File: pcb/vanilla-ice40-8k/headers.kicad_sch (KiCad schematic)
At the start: 4 parts, among them J1 QSH-060-01-L-D-A, J2 QSH-060-01-L-D-A, J3 QTH-060-01-L-D-A, J4 QTH-060-01-L-D-A

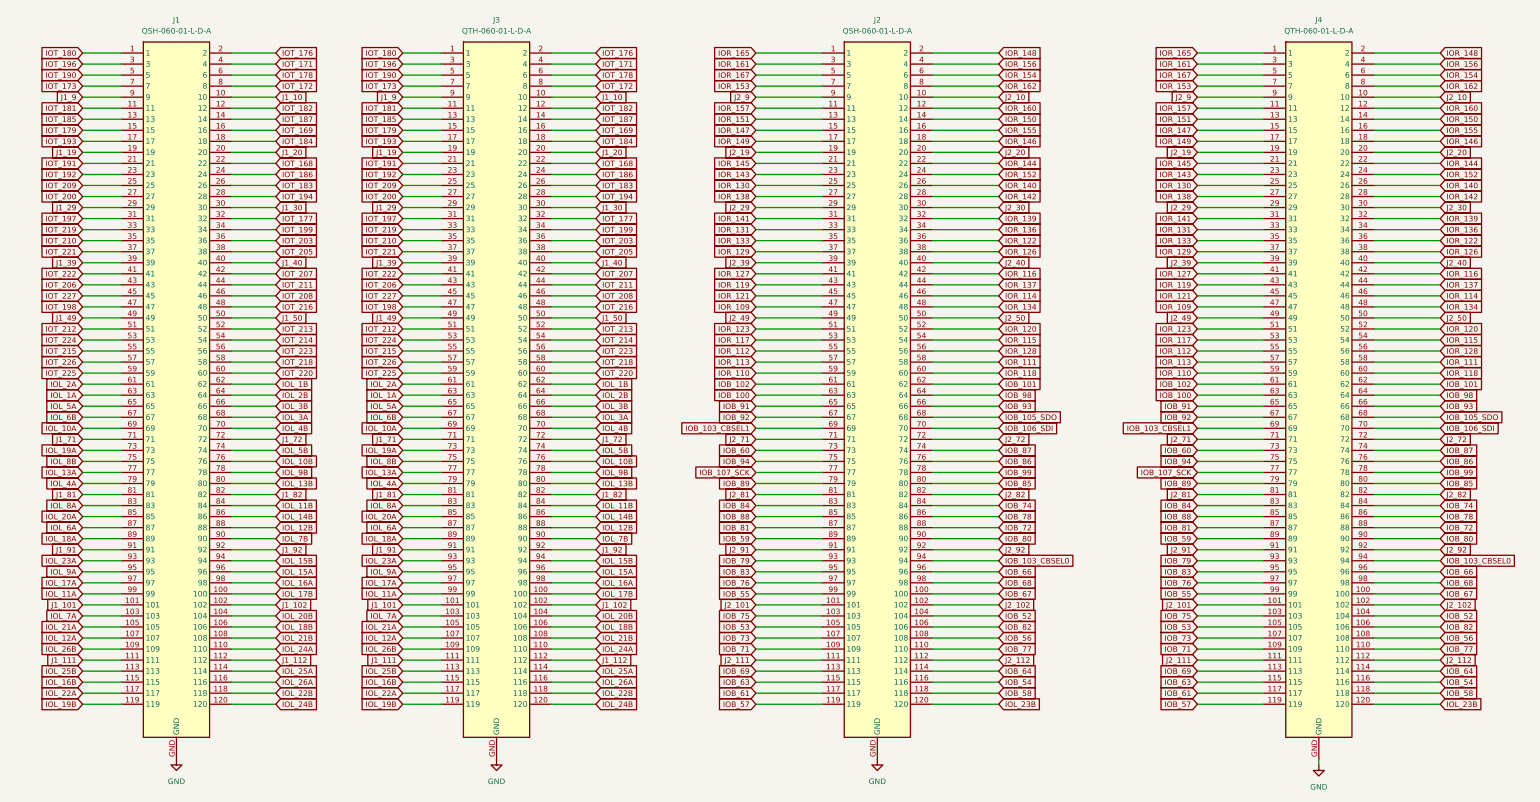
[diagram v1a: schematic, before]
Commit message: [hx8k][pcb] convert all components to custom lib
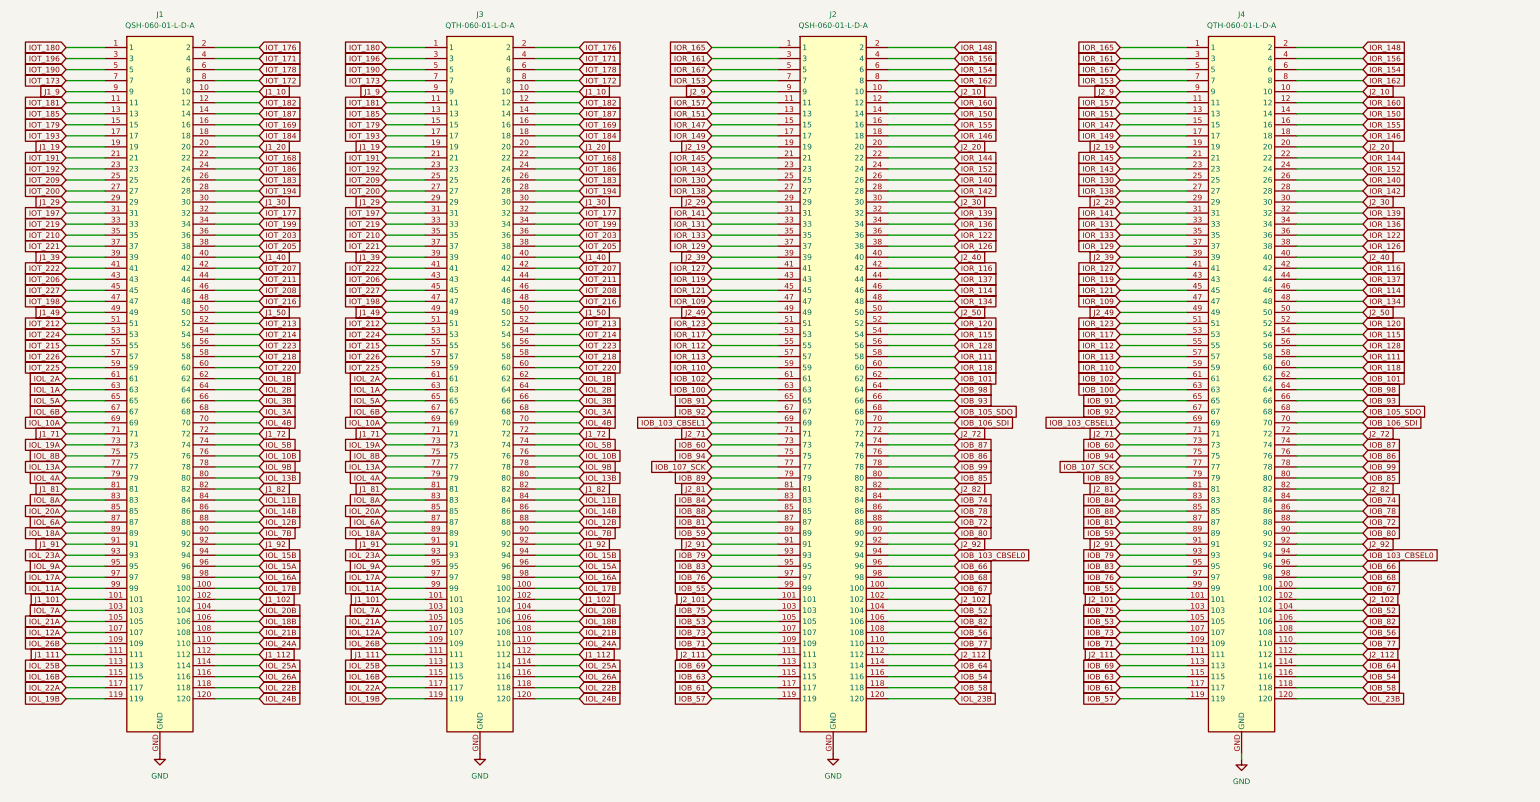
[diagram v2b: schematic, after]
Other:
- moved on the sheet: J1, J2, J3, J4

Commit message: [pcb][hx8k] add 3v3 to headers
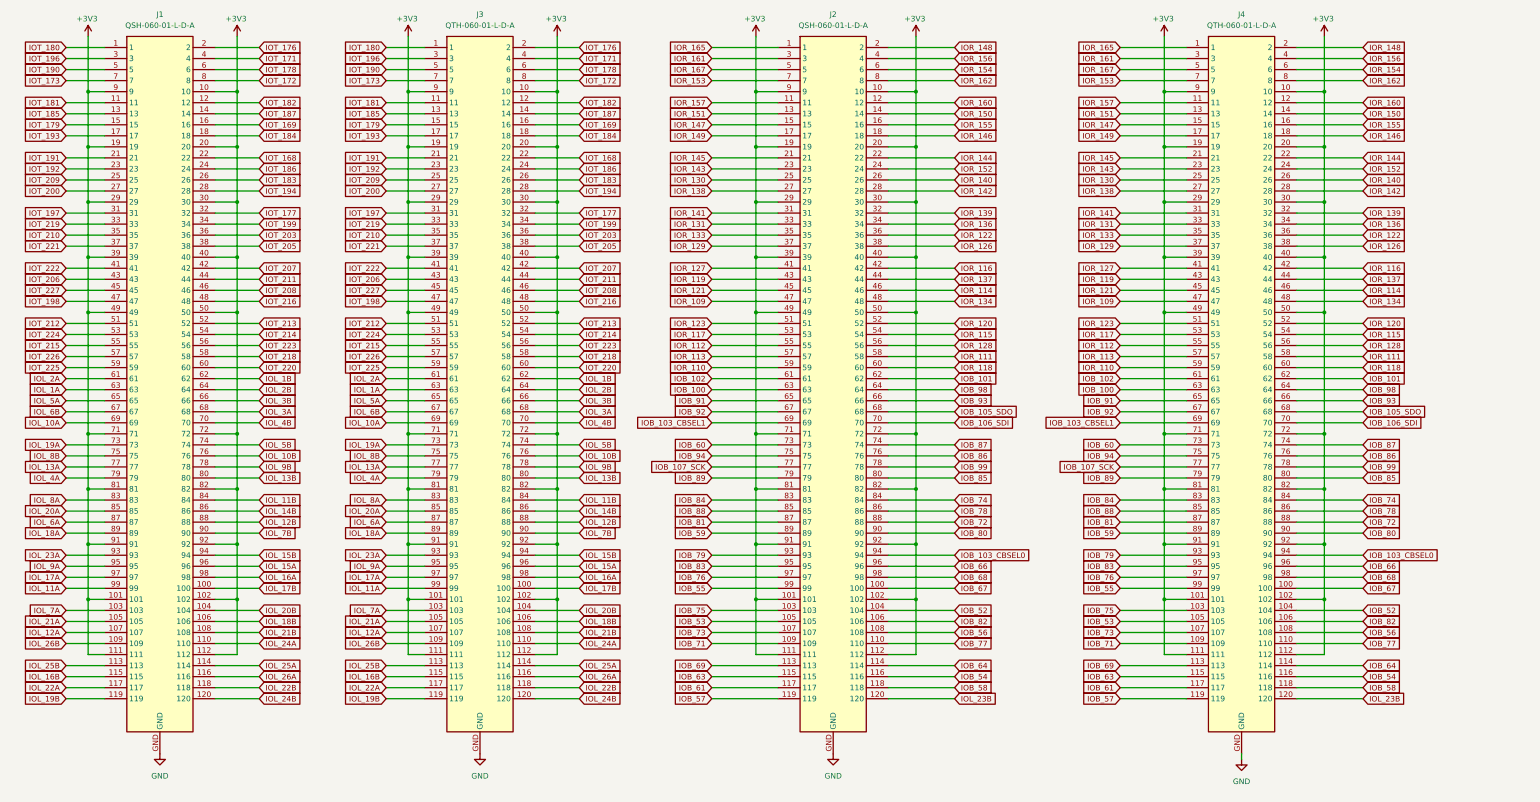
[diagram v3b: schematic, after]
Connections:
- net J1_101 is gone; now on net +3V3: J1.101, J3.101
- net J1_102 is gone; now on net +3V3: J1.102, J3.102
- net J1_111 is gone; now on net +3V3: J1.111, J3.111
- net J1_112 is gone; now on net +3V3: J1.112, J3.112
- net J1_19 is gone; now on net +3V3: J1.19, J3.19
- net J1_20 is gone; now on net +3V3: J1.20, J3.20
- net J1_29 is gone; now on net +3V3: J1.29, J3.29
- net J1_30 is gone; now on net +3V3: J1.30, J3.30
- net J1_39 is gone; now on net +3V3: J1.39, J3.39
- net J1_40 is gone; now on net +3V3: J1.40, J3.40
- net J1_49 is gone; now on net +3V3: J1.49, J3.49
- net J1_50 is gone; now on net +3V3: J1.50, J3.50
- net J1_71 is gone; now on net +3V3: J1.71, J3.71
- net J1_72 is gone; now on net +3V3: J1.72, J3.72
- net J1_81 is gone; now on net +3V3: J1.81, J3.81
- net J1_82 is gone; now on net +3V3: J1.82, J3.82
- net J1_9 is gone; now on net +3V3: J1.9, J3.9
- net J1_91 is gone; now on net +3V3: J1.91, J3.91
- net J1_92 is gone; now on net +3V3: J1.92, J3.92
- net J2_10 is gone; now on net +3V3: J2.10, J4.10
- net J2_101 is gone; now on net +3V3: J2.101, J4.101
- net J2_102 is gone; now on net +3V3: J2.102, J4.102
- net J2_111 is gone; now on net +3V3: J2.111, J4.111
- net J2_112 is gone; now on net +3V3: J2.112, J4.112
- net J2_19 is gone; now on net +3V3: J2.19, J4.19
- net J2_20 is gone; now on net +3V3: J2.20, J4.20
- net J2_29 is gone; now on net +3V3: J2.29, J4.29
- net J2_30 is gone; now on net +3V3: J2.30, J4.30
- net J2_39 is gone; now on net +3V3: J2.39, J4.39
- net J2_40 is gone; now on net +3V3: J2.40, J4.40
- net J2_49 is gone; now on net +3V3: J2.49, J4.49
- net J2_50 is gone; now on net +3V3: J2.50, J4.50
- net J2_71 is gone; now on net +3V3: J2.71, J4.71
- net J2_72 is gone; now on net +3V3: J2.72, J4.72
- net J2_81 is gone; now on net +3V3: J2.81, J4.81
- net J2_82 is gone; now on net +3V3: J2.82, J4.82
- net J2_9 is gone; now on net +3V3: J2.9, J4.9
- net J2_91 is gone; now on net +3V3: J2.91, J4.91
- net J2_92 is gone; now on net +3V3: J2.92, J4.92
- net J1_10 renamed +3V3

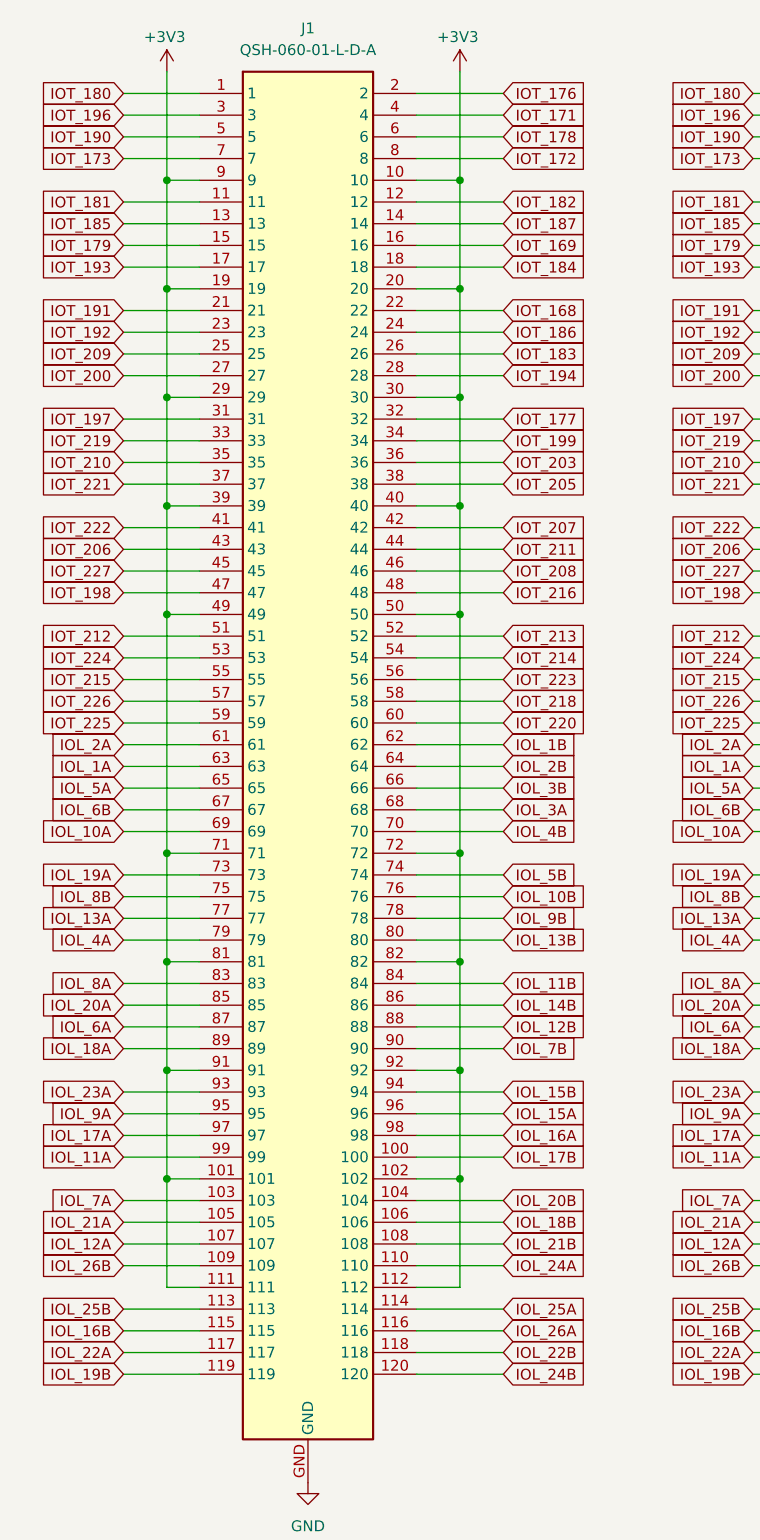
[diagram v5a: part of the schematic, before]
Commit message: [pcb][hx8k] add helper labels in header schematic
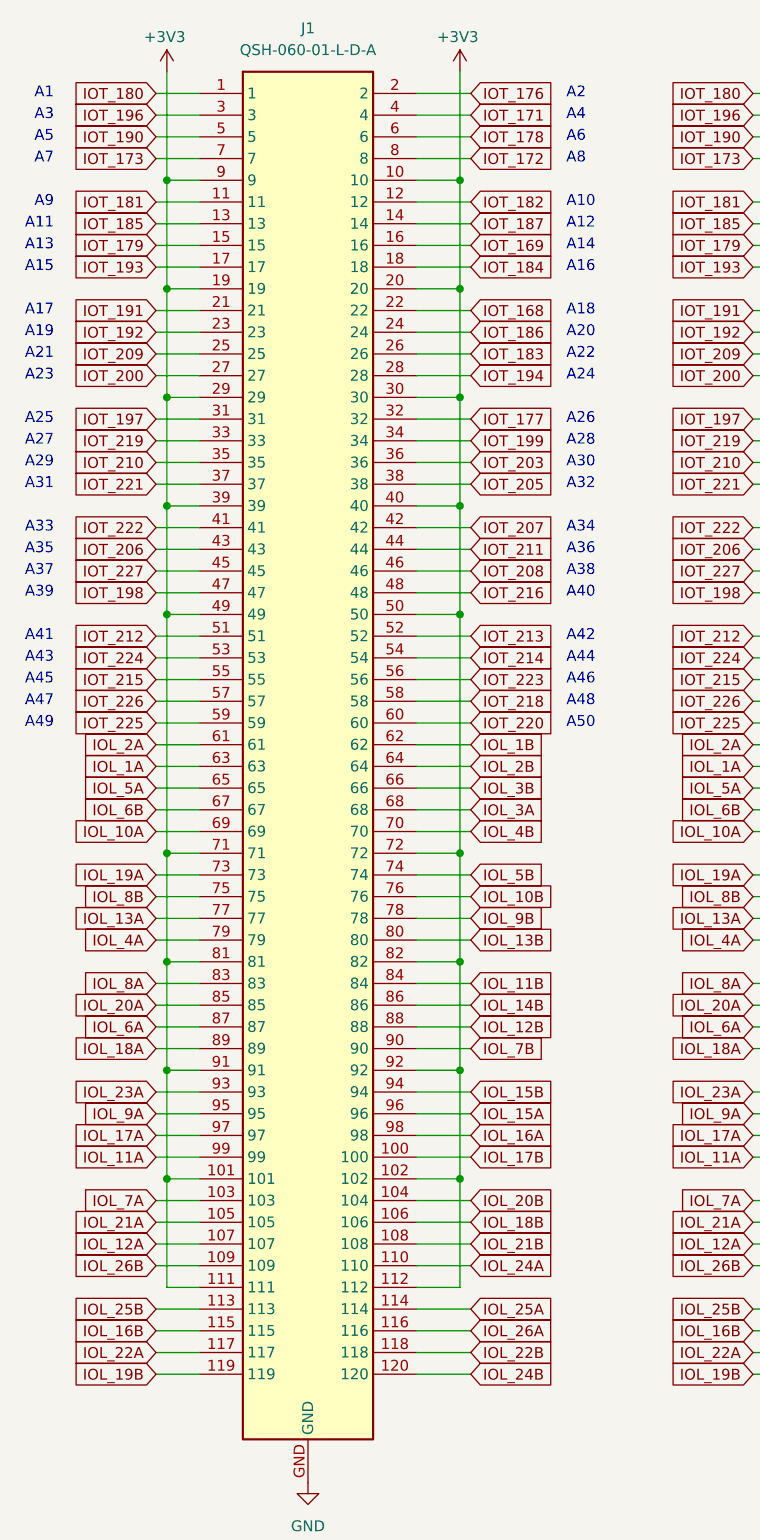
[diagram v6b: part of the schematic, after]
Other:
- note added: "A1"
- note added: "A10"
- note added: "A11"
- note added: "A12"
- note added: "A13"
- note added: "A14"
- note added: "A15"
- note added: "A16"
- note added: "A17"
- note added: "A18"
- note added: "A19"
- note added: "A2"
- note added: "A20"
- note added: "A21"
- note added: "A22"
- note added: "A23"
- note added: "A24"
- note added: "A25"
- note added: "A26"
- note added: "A27"
- note added: "A28"
- note added: "A29"
- note added: "A3"
- note added: "A30"
- note added: "A31"
- note added: "A32"
- note added: "A33"
- note added: "A34"
- note added: "A35"
- note added: "A36"
- note added: "A37"
- note added: "A38"
- note added: "A39"
- note added: "A4"
- note added: "A40"
- note added: "A41"
- note added: "A42"
- note added: "A43"
- note added: "A44"
- note added: "A45"
- note added: "A46"
- note added: "A47"
- note added: "A48"
- note added: "A49"
- note added: "A5"
- note added: "A50"
- note added: "A6"
- note added: "A7"
- note added: "A8"
- note added: "A9"

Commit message: [pcb][hx8k] add remaining helper labels
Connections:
- net IOB_103_CBSEL1 renamed IOB_104_CBSEL1
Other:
- note added: "B1"
- note added: "B10"
- note added: "B11"
- note added: "B12"
- note added: "B13"
- note added: "B14"
- note added: "B15"
- note added: "B16"
- note added: "B17"
- note added: "B18"
- note added: "B19"
- note added: "B2"
- note added: "B20"
- note added: "B21"
- note added: "B22"
- note added: "B23"
- note added: "B24"
- note added: "B25"
- note added: "B26"
- note added: "B27"
- note added: "B28"
- note added: "B29"
- note added: "B3"
- note added: "B30"
- note added: "B31"
- note added: "B32"
- note added: "B33"
- note added: "B34"
- note added: "B35"
- note added: "B36"
- note added: "B37"
- note added: "B38"
- note added: "B39"
- note added: "B4"
- note added: "B40"
- note added: "B41"
- note added: "B42"
- note added: "B43"
- note added: "B44"
- note added: "B45"
- note added: "B46"
- note added: "B47"
- note added: "B48"
- note added: "B49"
- note added: "B5"
- note added: "B50"
- note added: "B6"
- note added: "B7"
- note added: "B8"
- note added: "B9"
- note added: "C1"
- note added: "C10"
- note added: "C11"
- note added: "C12"
- note added: "C13"
- note added: "C14"
- note added: "C15"
- note added: "C16"
- note added: "C17"
- note added: "C18"
- note added: "C19"
- note added: "C2"
- note added: "C20"
- note added: "C21"
- note added: "C22"
- note added: "C23"
- note added: "C24"
- note added: "C25"
- note added: "C26"
- note added: "C27"
- note added: "C28"
- note added: "C29"
- note added: "C3"
- note added: "C30"
- note added: "C31"
- note added: "C32"
- note added: "C33"
- note added: "C34"
- note added: "C35"
- note added: "C36"
- note added: "C37"
- note added: "C38"
- note added: "C39"
- note added: "C4"
- note added: "C40"
- note added: "C41"
- note added: "C42"
- note added: "C43"
- note added: "C44"
- note added: "C45"
- note added: "C46"
- note added: "C47"
- note added: "C48"
- note added: "C49"
- note added: "C5"
- note added: "C50"
- note added: "C6"
- note added: "C7"
- note added: "C8"
- note added: "C9"
- note added: "D1"
- note added: "D10"
- note added: "D11"
- note added: "D12"
- note added: "D13"
- note added: "D14"
- note added: "D15"
- note added: "D16"
- note added: "D17"
- note added: "D18"
- note added: "D19"
- note added: "D2"
- note added: "D20"
- note added: "D21"
- note added: "D22"
- note added: "D23"
- note added: "D24"
- note added: "D25"
- note added: "D26"
- note added: "D27"
- note added: "D28"
- note added: "D29"
- note added: "D3"
- note added: "D30"
- note added: "D31"
- note added: "D32"
- note added: "D33"
- note added: "D34"
- note added: "D35"
- note added: "D36"
- note added: "D37"
- note added: "D38"
- note added: "D39"
- note added: "D4"
- note added: "D40"
- note added: "D41"
- note added: "D42"
- note added: "D43"
- note added: "D44"
- note added: "D45"
- note added: "D46"
- note added: "D47"
- note added: "D48"
- note added: "D49"
- note added: "D5"
- note added: "D50"
- note added: "D6"
- note added: "D7"
- note added: "D8"
- note added: "D9"
